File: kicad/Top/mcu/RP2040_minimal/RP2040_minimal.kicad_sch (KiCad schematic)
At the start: 37 parts, among them J2 Conn_01x02, U2 W25Q128JVS, U3 RP2040, Y1 ABLS-12.000MHZ-B4-T

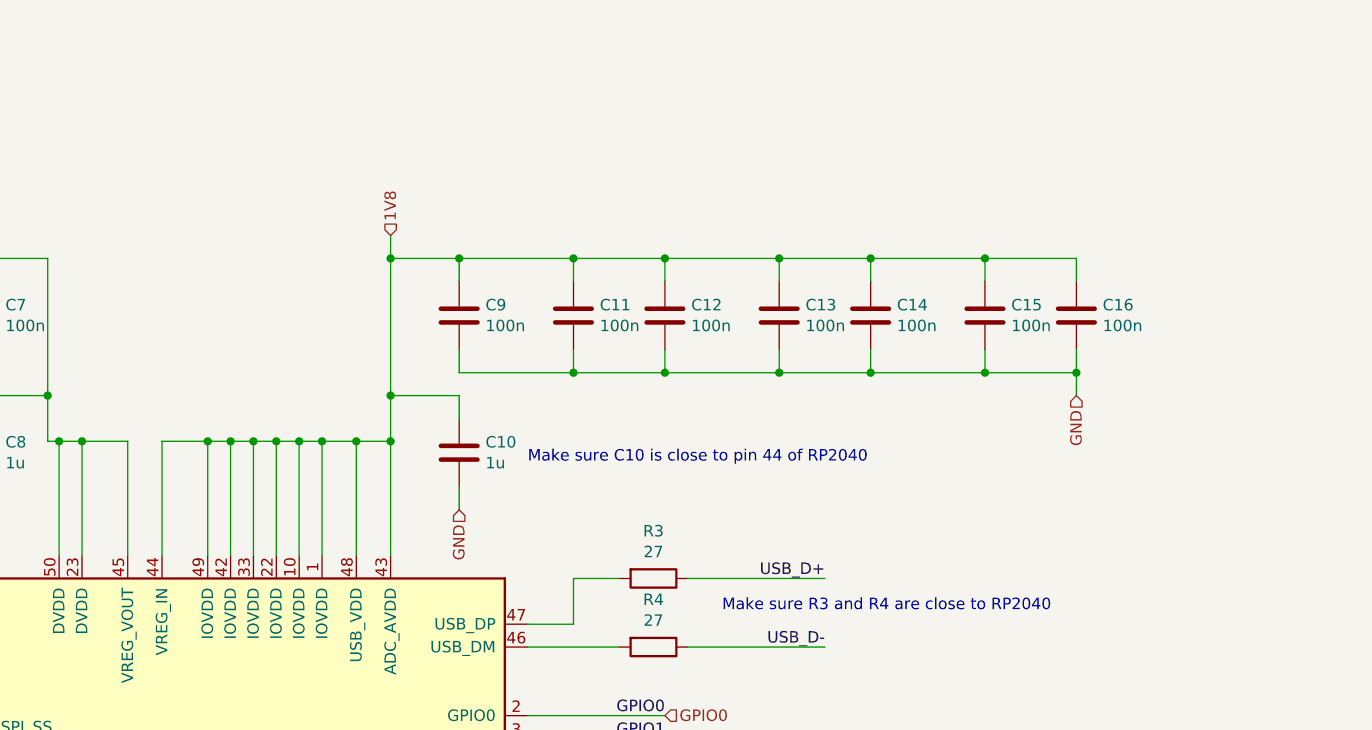
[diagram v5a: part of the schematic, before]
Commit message: Seperated and added 3V3 to MCU for USB and AVD supply
As per Sections 2.9.4, 2.9.5 and 2.9.7.3 of the rp2040 datasheet
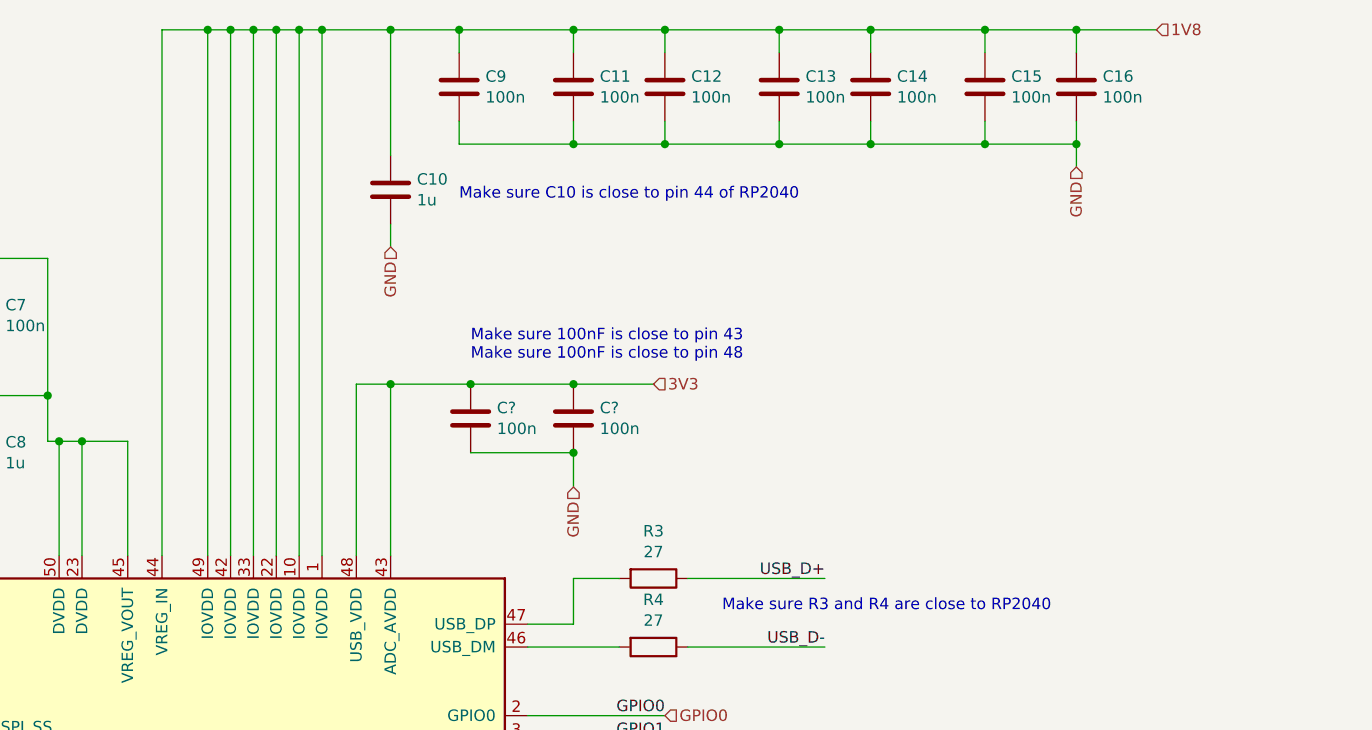
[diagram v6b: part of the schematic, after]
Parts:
- added C? (x2): 100n, Capacitor_SMD:C_0402_1005Metric, symbol Device:C
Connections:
- net 1V8: no longer U3.43 (ADC_AVDD), U3.48 (USB_VDD)
- net 3V3: now also U3.43 (ADC_AVDD), U3.48 (USB_VDD), C?.1, C?.1
- net GND: now also C?.2, C?.2
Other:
- note added: "Make sure 100nF is close to pin 43 Make sure 100nF is close to pin 48"
- moved on the sheet: C10, C11, C12, C13, C14, C15, C16, C9

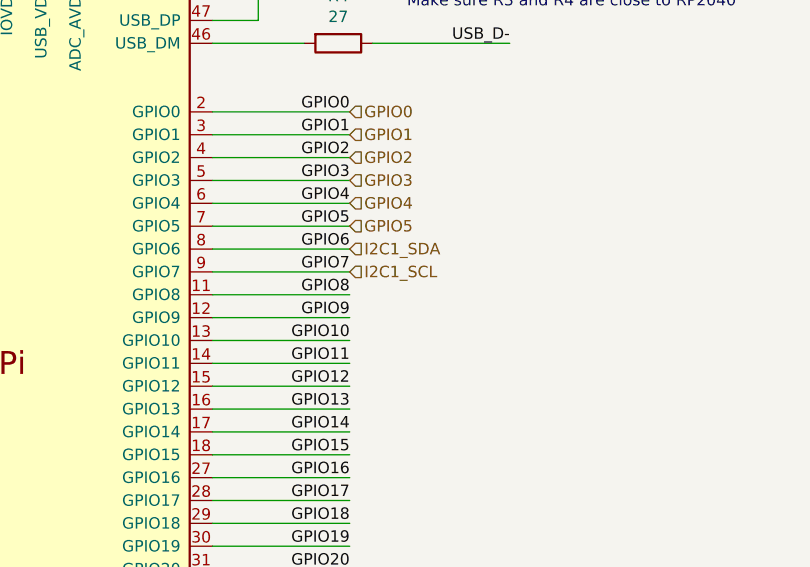
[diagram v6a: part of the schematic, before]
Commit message: All VIO now on 1V8
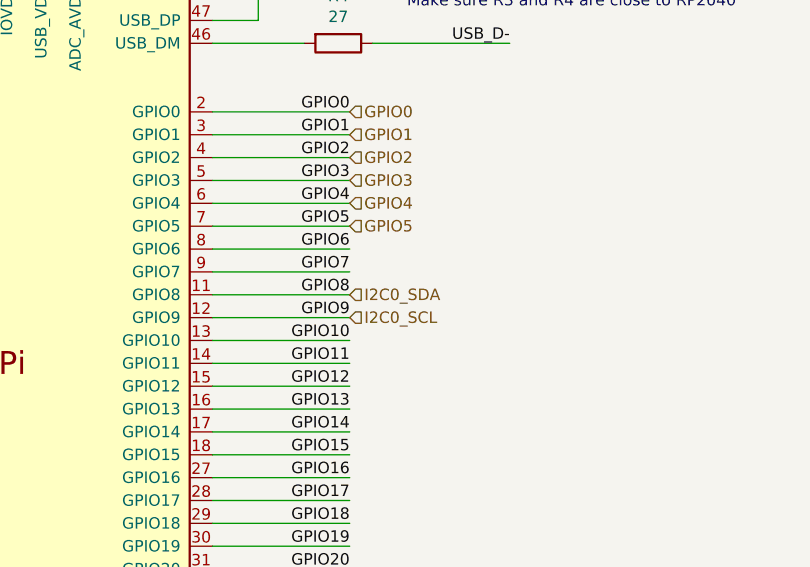
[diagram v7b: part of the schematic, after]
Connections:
- net GPIO8 renamed I2C0_SDA
- net GPIO9 renamed I2C0_SCL
- net I2C1_SCL renamed GPIO7
- net I2C1_SDA renamed GPIO6
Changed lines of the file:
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@@
-    (effects (font (size 1.27 1.27)) (justify left))
-  )
-  (hierarchical_label "I2C1_SCL" (shape input) (at 246.38 129.54 0)
     (effects (font (size 1.27 1.27)) (justify left))
   )
@@
   (hierarchical_label "GND" (shape input) (at 292.1 50.8 270)
     (effects (font (size 1.27 1.27)) (justify right))
-  )
-  (hierarchical_label "I2C1_SDA" (shape input) (at 246.38 127 0)
-    (effects (font (size 1.27 1.27)) (justify left))
   )
   (hierarchical_label "GPIO0" (shape input) (at 246.38 111.76 0)
@@
     (effects (font (size 1.27 1.27)) (justify right))
   )
+  (hierarchical_label "I2C0_SDA" (shape input) (at 246.38 132.08 0)
+    (effects (font (size 1.27 1.27)) (justify left))
+  )
   (hierarchical_label "GND" (shape input) (at 45.72 231.14 270)
     (effects (font (size 1.27 1.27)) (justify right))
   )
+  (hierarchical_label "I2C0_SCL" (shape input) (at 246.38 134.62 0)
+    (effects (font (size 1.27 1.27)) (justify left))
+  )
   (hierarchical_label "GND" (shape input) (at 78.74 149.86 270)

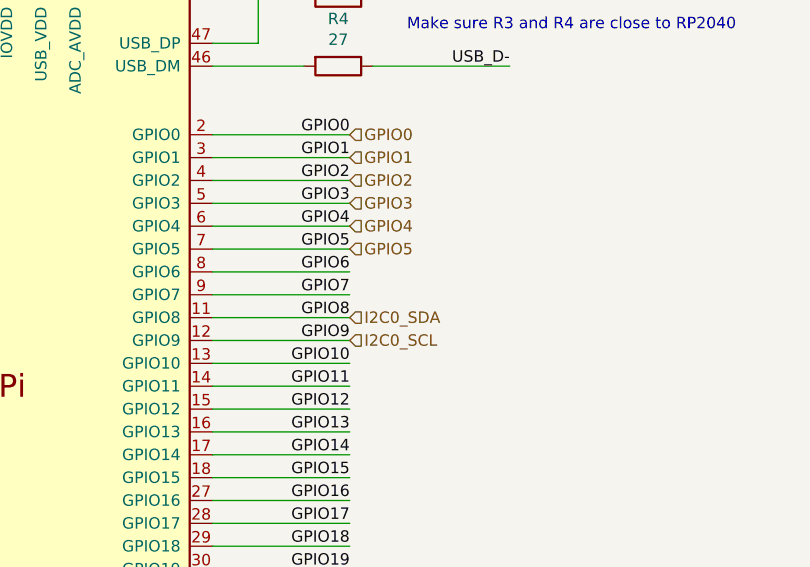
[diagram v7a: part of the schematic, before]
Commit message: Renamed nets for I2C buses and connected via buses
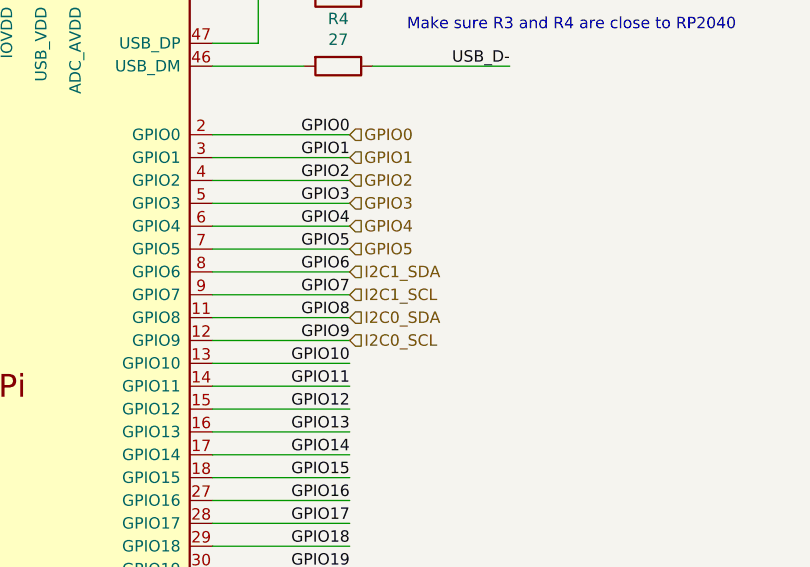
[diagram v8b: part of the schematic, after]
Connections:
- net GPIO6 renamed I2C1_SDA
- net GPIO7 renamed I2C1_SCL
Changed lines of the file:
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@@
     (effects (font (size 1.27 1.27)) (justify right))
+  )
+  (hierarchical_label "I2C1_SDA" (shape input) (at 246.38 127 0)
+    (effects (font (size 1.27 1.27)) (justify left))
   )
   (hierarchical_label "GPIO2" (shape input) (at 246.38 116.84 0)
@@
     (effects (font (size 1.27 1.27)) (justify right))
   )
+  (hierarchical_label "I2C1_SCL" (shape input) (at 246.38 129.54 0)
+    (effects (font (size 1.27 1.27)) (justify left))
+  )
   (hierarchical_label "GND" (shape input) (at 383.54 129.54 270)
